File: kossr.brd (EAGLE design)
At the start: 50 x 39 mm, 18 parts, among them T1 BTA12-600, U1 TINY45-20-DIP

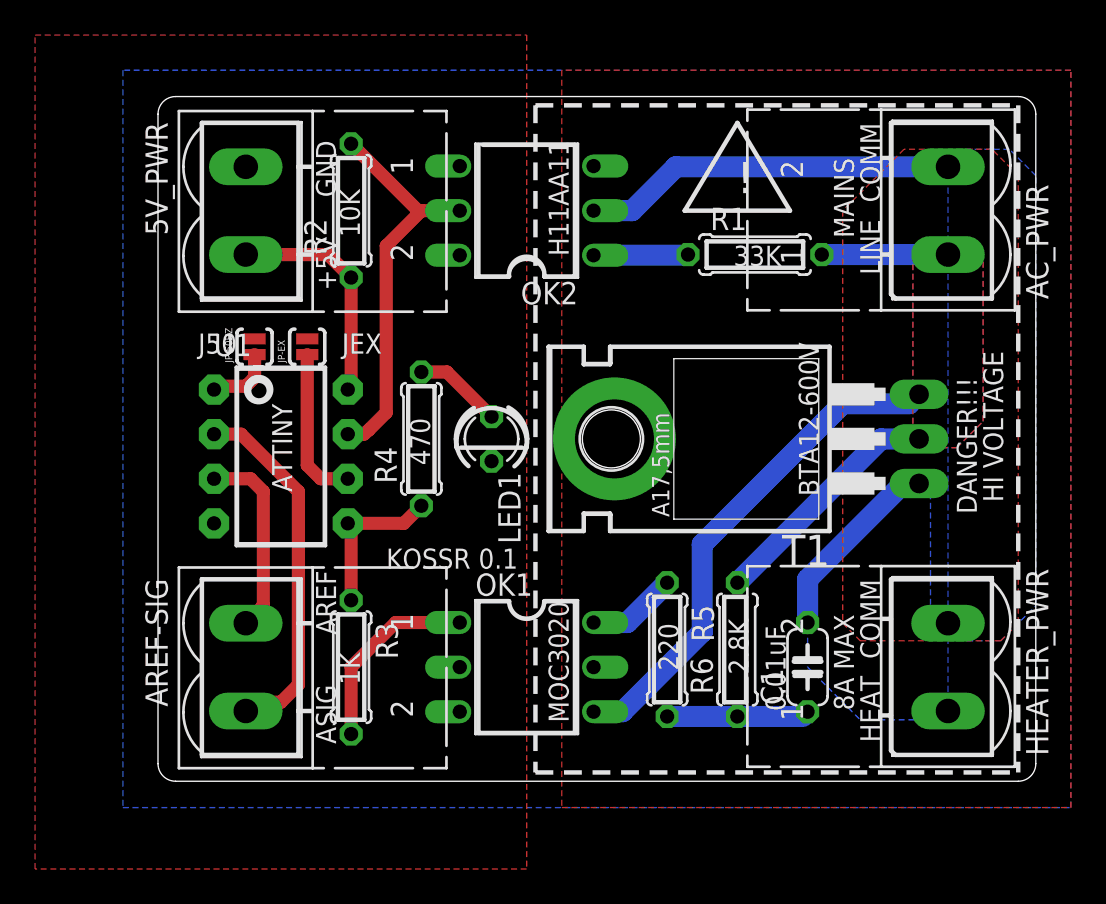
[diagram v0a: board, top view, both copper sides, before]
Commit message: update to kossr 0.2
adds input r/c filter
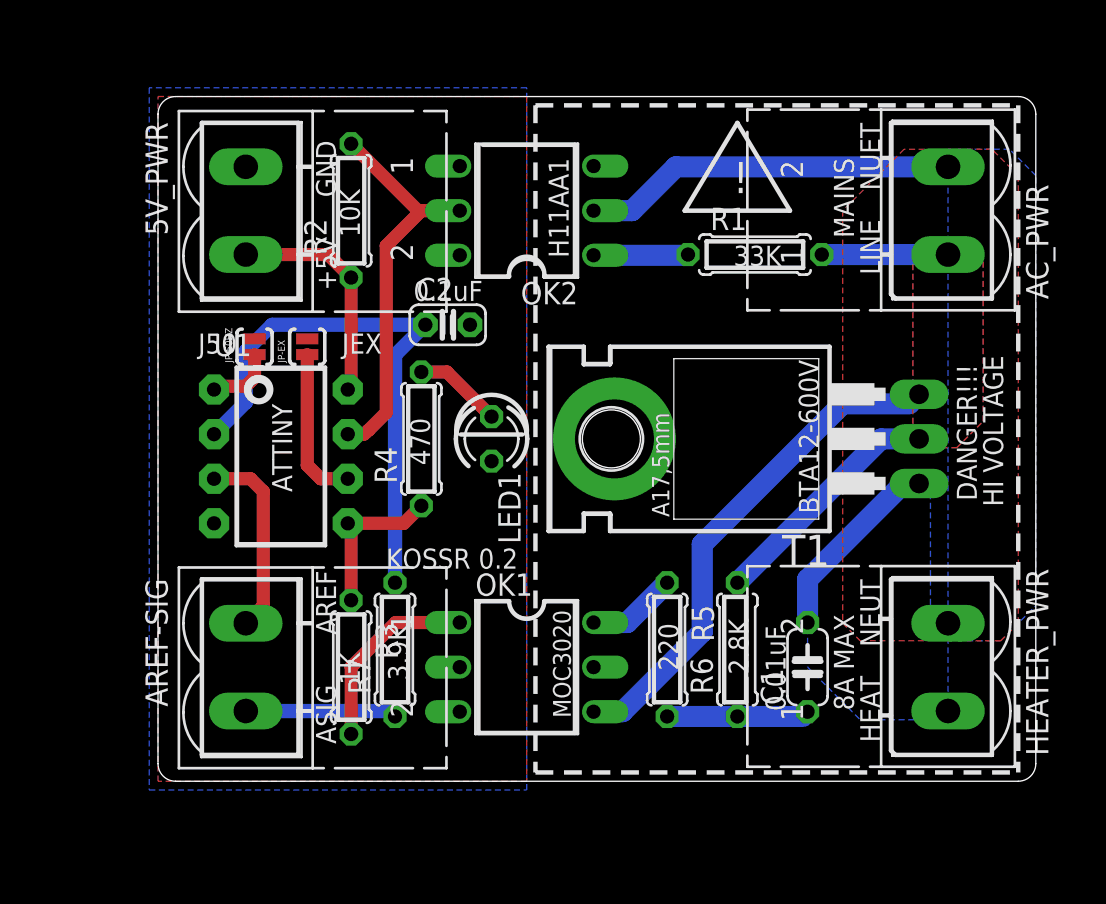
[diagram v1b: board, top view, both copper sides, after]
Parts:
- added C2: 0.1uF, adafruit:C025-024X044
- added R7: 3.9K, rcl:0207/7
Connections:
- new net PWM_FILTERED: C2.1, R7.2, U1.2
- net GND: now also C2.2
- net PWM_IN: now also R7.1; no longer U1.2
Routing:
- net PWM_FILTERED: track 0.00 -> 31.7 mm
- net PWM_IN: track 20.8 -> 8.63 mm
- added copper zone on layer 16, net GND
- removed copper zone on layer 1, net N$4
- removed copper zone on layer 16, net N$4
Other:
- board text added: "0.1uF"
- board text added: "3.9K"
- board text added: "H11AA1"
- board text added: "KOSSR 0.2"
- board text added: "NEUT"
- board text added: "NUET"
- board text removed: "COMM"
- board text removed: "H11AA11"
- board text removed: "KOSSR 0.1"
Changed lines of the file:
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@@
 <?xml version="1.0" encoding="utf-8"?>
 <!DOCTYPE eagle SYSTEM "eagle.dtd">
-<eagle version="6.3">
+<eagle version="6.6.0">
 <drawing>
 <settings>
@@
 <layer number="17" name="Pads" color="2" fill="1" visible="yes" active="yes"/>
 <layer number="18" name="Vias" color="2" fill="1" visible="yes" active="yes"/>
-<layer number="19" name="Unrouted" color="6" fill="1" visible="no" active="yes"/>
+<layer number="19" name="Unrouted" color="6" fill="1" visible="yes" active="yes"/>
 <layer number="20" name="Dimension" color="15" fill="1" visible="yes" active="yes"/>
 <layer number="21" name="tPlace" color="7" fill="1" visible="no" active="yes"/>
@@
 <layer number="27" name="tValues" color="7" fill="1" visible="no" active="yes"/>
 <layer number="28" name="bValues" color="7" fill="1" visible="no" active="yes"/>
-<layer number="29" name="tStop" color="7" fill="3" visible="yes" active="yes"/>
-<layer number="30" name="bStop" color="7" fill="6" visible="yes" active="yes"/>
+<layer number="29" name="tStop" color="7" fill="3" visible="no" active="yes"/>
+<layer number="30" name="bStop" color="7" fill="6" visible="no" active="yes"/>
 <layer number="31" name="tCream" color="14" fill="9" visible="no" active="yes"/>
 <layer number="32" name="bCream" color="11" fill="9" visible="no" active="yes"/>
@@
 <text x="15.5" y="18" size="1.143" layer="114" ratio="17" distance="47" rot="R90">470</text>
 <text x="28.5" y="9" size="1.143" layer="114" ratio="17" distance="47" rot="R270">220</text>
-<text x="22.25" y="10.25" size="1.143" layer="114" ratio="17" distance="47" rot="R270">MOC3020</text>
-<text x="22.25" y="36.5" size="1.143" layer="114" ratio="17" distance="47" rot="R270">H11AA11</text>
-<text x="36.5" y="25" size="1.143" layer="114" ratio="17" distance="47" rot="R270">BTA12-600V</text>
+<text x="22.5" y="9.75" size="1.016" layer="114" ratio="17" distance="47" rot="R270">MOC3020</text>
+<text x="22.25" y="35.5" size="1.143" layer="114" ratio="17" distance="47" rot="R270">H11AA1</text>
+<text x="36.5" y="24" size="1.143" layer="114" ratio="17" distance="47" rot="R270">BTA12-600V</text>
 <text x="6.5" y="21.5" size="1.143" layer="114" ratio="17" distance="47" rot="R270">ATTINY</text>
 <text x="40" y="32" size="1.143" layer="114" ratio="17" distance="47" rot="R270">LINE</text>
-<text x="40" y="37.5" size="1.143" layer="114" ratio="17" distance="47" rot="R270">COMM</text>
+<text x="40" y="37.5" size="1.143" layer="114" ratio="17" distance="47" rot="R270">NUET</text>
 <text x="40" y="6" size="1.143" layer="114" ratio="17" distance="47" rot="R270">HEAT</text>
-<text x="40" y="11.5" size="1.143" layer="114" ratio="17" distance="47" rot="R270">COMM</text>
+<text x="40" y="11.5" size="1.143" layer="114" ratio="17" distance="47" rot="R270">NEUT</text>
 <text x="35.75" y="4" size="1.143" layer="114" ratio="17" distance="47" rot="R90">0.01uF</text>
 <text x="9" y="36.5" size="1.143" layer="114" ratio="17" distance="47" rot="R270">GND</text>
@@
 <text x="9" y="12" size="1.143" layer="114" ratio="17" distance="47" rot="R270">AREF</text>
 <text x="9" y="5.5" size="1.143" layer="114" ratio="17" distance="47" rot="R270">ASIG</text>
-<text x="47" y="24.5" size="1.143" layer="114" ratio="17" distance="47" rot="R270">HI VOLTAGE</text>
-<text x="45.5" y="23" size="1.143" layer="114" ratio="17" distance="47" rot="R270">DANGER!!!</text>
+<text x="47" y="24.25" size="1.143" layer="114" ratio="17" distance="47" rot="R270">HI VOLTAGE</text>
+<text x="45.5" y="23.75" size="1.143" layer="114" ratio="17" distance="47" rot="R270">DANGER!!!</text>
 <wire x1="21.5" y1="38.5" x2="21.5" y2="0.5" width="0.254" layer="114" style="shortdash"/>
 <wire x1="21.5" y1="0.5" x2="49" y2="0.5" width="0.254" layer="114" style="shortdash"/>
 <wire x1="21.5" y1="38.5" x2="49" y2="38.5" width="0.254" layer="114" style="shortdash"/>
 <wire x1="49" y1="38.5" x2="49" y2="0.5" width="0.254" layer="114" style="shortdash"/>
-<text x="20.5" y="13.25" size="1.143" layer="114" ratio="17" distance="47" rot="R180">KOSSR 0.1</text>
+<text x="20.5" y="13.25" size="1.143" layer="114" ratio="17" distance="47" rot="R180">KOSSR 0.2</text>
 <text x="38.5" y="9.5" size="1.143" layer="114" ratio="17" distance="47" rot="R270">8A MAX</text>
 <rectangle x1="23" y1="15" x2="37" y2="25" layer="29"/>
@@
 <wire x1="41.75" y1="1.75" x2="42" y2="1.5" width="0.254" layer="114"/>
 <wire x1="42" y1="1.5" x2="47.5" y2="1.5" width="0.254" layer="114"/>
-<wire x1="20.75" y1="19" x2="17.25" y2="19" width="0.254" layer="114"/>
-<wire x1="17" y1="19" x2="21" y2="19" width="0.254" layer="114" curve="-194.036243"/>
+<wire x1="20.75" y1="19.75" x2="17.25" y2="19.75" width="0.254" layer="114"/>
+<wire x1="17" y1="19.75" x2="21" y2="19.75" width="0.254" layer="114" curve="-194.036243"/>
 <wire x1="31.25" y1="30.75" x2="31.25" y2="29.25" width="0.254" layer="114"/>
 <wire x1="31.25" y1="29.25" x2="36.75" y2="29.25" width="0.254" layer="114"/>
@@
 <wire x1="30" y1="32.5" x2="36" y2="32.5" width="0.254" layer="114"/>
 <wire x1="36" y1="32.5" x2="33" y2="37.5" width="0.254" layer="114"/>
-<text x="33" y="33.5" size="1.778" layer="114">!</text>
+<text x="32.75" y="33.5" size="1.778" layer="114">!</text>
 <wire x1="2.5" y1="37.5" x2="2.5" y2="27.5" width="0.254" layer="114"/>
 <wire x1="2.5" y1="11.5" x2="2.5" y2="1.5" width="0.254" layer="114"/>
@@
 <wire x1="47.5" y1="37.5" x2="47.5" y2="27.5" width="0.254" layer="114"/>
 <text x="38.5" y="35.5" size="1.143" layer="114" ratio="17" distance="47" rot="R270">MAINS</text>
+<text x="14.25" y="5.75" size="1.143" layer="114" ratio="17" distance="47" rot="R90">3.9K</text>
+<wire x1="12.75" y1="10.5" x2="12.75" y2="4.5" width="0.254" layer="114"/>
+<wire x1="14.25" y1="4.5" x2="14.25" y2="10.5" width="0.254" layer="114"/>
+<wire x1="12.75" y1="10.5" x2="14.25" y2="10.5" width="0.254" layer="114"/>
+<wire x1="14.25" y1="4.5" x2="12.75" y2="4.5" width="0.254" layer="114"/>
+<wire x1="16.25" y1="26.5" x2="16.25" y2="25.5" width="0.254" layer="114"/>
+<wire x1="16.75" y1="26.5" x2="16.75" y2="25.5" width="0.254" layer="114"/>
+<text x="18.5" y="28.5" size="1.143" layer="114" ratio="17" distance="47" rot="R180">0.1uF</text>
 </plain>
 <attributes>
@@
 <element name="JP-50HZ" library="SparkFun-Retired" package="SJ_2S-NO" value="" x="5.5" y="24.75" rot="R90"/>
 <element name="JP-EX" library="SparkFun-Retired" package="SJ_2S-NO" value="" x="8.5" y="24.75" rot="R90"/>
+<element name="C2" library="adafruit" package="C025-024X044" value="0.1uF" x="16.5" y="26"/>
+<element name="R7" library="rcl" package="0207/7" value="3.9K" x="13.5" y="7.5" rot="R90"/>
 </elements>
 <signals>
@@
 <contactref element="JP-EX" pad="2"/>
 <polygon width="0.508" layer="1" rank="3">
-<vertex x="-7" y="42.5"/>
-<vertex x="21" y="42.5"/>
-<vertex x="21" y="-5"/>
-<vertex x="-7" y="-5"/>
+<vertex x="0" y="39"/>
+<vertex x="21" y="39"/>
+<vertex x="21" y="0"/>
+<vertex x="0" y="0"/>
 </polygon>
 <contactref element="LED1" pad="K"/>
+<contactref element="C2" pad="2"/>
+<polygon width="0.5" layer="16" isolate="0.5" rank="6">
+<vertex x="-0.5" y="39.5"/>
+<vertex x="-0.5" y="-0.5"/>
+<vertex x="21" y="-0.5"/>
+<vertex x="21" y="39.5"/>
+</polygon>
 </signal>
 <signal name="N$1" class="2">
@@
 <signal name="PWM_IN">
 <contactref element="AREF-SIG" pad="2"/>
-<contactref element="U1" pad="2"/>
-<wire x1="5" y1="4" x2="5.5" y2="4.5" width="0.75" layer="1"/>
-<wire x1="5.5" y1="4.5" x2="7" y2="4.5" width="0.75" layer="1"/>
-<wire x1="7" y1="4.5" x2="8" y2="5.5" width="0.75" layer="1"/>
-<wire x1="8" y1="5.5" x2="8" y2="16.5" width="0.75" layer="1"/>
-<wire x1="8" y1="16.5" x2="4.73" y2="19.77" width="0.75" layer="1"/>
-<wire x1="4.73" y1="19.77" x2="3.19" y2="19.77" width="0.75" layer="1"/>
+<contactref element="R7" pad="1"/>
+<wire x1="5" y1="4" x2="13.19" y2="4" width="0.8128" layer="16"/>
+<wire x1="13.19" y1="4" x2="13.5" y2="3.69" width="0.8128" layer="16"/>
 </signal>
 <signal name="ACN" class="1">
@@
 <signal name="N$4">
 <via x="26" y="19.5" extent="1-16" drill="4.5" diameter="7" alwaysstop="yes"/>
-<polygon width="0.5" layer="16" isolate="0.5" rank="6">
-<vertex x="-2" y="40.5"/>
-<vertex x="-2" y="-1.5"/>
-<vertex x="52" y="-1.5"/>
-<vertex x="52" y="40.5"/>
-</polygon>
-<polygon width="0.5" layer="1" isolate="0.5" rank="6">
-<vertex x="23" y="40.5"/>
-<vertex x="23" y="-1.5"/>
-<vertex x="52" y="-1.5"/>
-<vertex x="52" y="40.5"/>
-</polygon>
+</signal>
+<signal name="PWM_FILTERED">
+<contactref element="C2" pad="1"/>
+<contactref element="R7" pad="2"/>
+<contactref element="U1" pad="2"/>
+<wire x1="15.23" y1="26" x2="6.5" y2="26" width="0.8128" layer="16"/>
+<wire x1="6.5" y1="26" x2="5" y2="24.5" width="0.8128" layer="16"/>
+<wire x1="5" y1="24.5" x2="5" y2="21.58" width="0.8128" layer="16"/>
+<wire x1="5" y1="21.58" x2="3.19" y2="19.77" width="0.8128" layer="16"/>
+<wire x1="13.5" y1="11.31" x2="13.5" y2="24.27" width="0.8128" layer="16"/>
+<wire x1="13.5" y1="24.27" x2="15.23" y2="26" width="0.8128" layer="16"/>
 </signal>
 </signals>
